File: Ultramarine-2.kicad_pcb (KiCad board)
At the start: 2 copper layers, 135 x 122.8 mm, 148 parts, among them SW1 SW_Push, SW10 SW_Push, SW11 SW_Push, SW12 SW_Push, SW13 SW_Push, SW14 Command 2, SW15 SW_Push, SW16 SW_Push, SW17 SW_Push, SW18 SW_Push, SW19 SW_Push, SW2 SW_Push, SW20 SW_Push, SW21 Command 3, SW22 SW_Push, SW23 SW_Push, SW24 SW_Push, SW25 SW_Push, SW26 SW_Push, SW27 SW_Push, SW28 SW_Push, SW29 SW_Push, SW3 SW_Push, SW30 SW_Push, SW31 Extra, SW32 SW_Push, SW33 SW_Push, SW34 SW_Push, SW35 RotaryEncoder_Switch, SW36 Reset, SW4 SW_Push, SW5 SW_Push, SW6 SW_Push, SW7 Command 1, SW8 SW_Push, SW9 SW_Push

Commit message: Added Qi charging unit
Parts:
- removed D100, D101, D102, D103, D104, D105, D21, D78, D79, D80, D81, D82, D83, D84, D99: D, Diode_SMD:D_SOD-123
- removed D14, D67, D68, D69, D7, D70, D71, D72, D73, D74, D75, D76, D77, D85, D86, D87, D88, D89, D90, D91, D92, D93, D94, D95, D96, D97, D98: SK6812MINI, LED_SMD:LED_SK6812MINI_PLCC4_3.5x3.5mm_P1.75mm
- removed SW14: Command 2, Button_Switch_THT:SW_Tactile_SPST_Angled_PTS645Vx58-2LFS
- removed SW21: Command 3, Button_Switch_THT:SW_Tactile_SPST_Angled_PTS645Vx58-2LFS
- removed SW7: Command 1, Button_Switch_THT:SW_Tactile_SPST_Angled_PTS645Vx58-2LFS
- added J1: OLED, Connector_PinSocket_2.54mm:PinSocket_1x04_P2.54mm_Vertical, F.Cu at (207.2, 80.0)
- added J2: TRRS, Ultramarine-2:MJ-4PP-9, F.Cu at (221.0, 52.0)
- added JP5: Power1, Jumper:SolderJumper-3_P2.0mm_Open_TrianglePad1.0x1.5mm, F.Cu at (161.5, -26.2)
- added JP6: Batt.1, Jumper:SolderJumper-3_P2.0mm_Open_TrianglePad1.0x1.5mm, F.Cu at (161.5, -18.5)
- added JP7: Power1, Jumper:SolderJumper-3_P2.0mm_Open_TrianglePad1.0x1.5mm, F.Cu at (161.5, -22.4)
- added JP8: Batt.2, Jumper:SolderJumper-3_P2.0mm_Open_TrianglePad1.0x1.5mm, F.Cu at (161.5, -14.7)
- added R1: 10K, Resistor_SMD:R_0603_1608Metric, F.Cu at (167.0, -14.5)
- added R2: 10K, Resistor_SMD:R_0603_1608Metric, F.Cu at (167.0, -12.0)
- added REF**: Stabilizer_Cherry_MX_2.00u, PCM_Mounting_Keyboard_Stabilizer:Stabilizer_Cherry_MX_2.00u, F.Cu at (202.9, 134.9)
- added U2: ~, Ultramarine-2:BLE Micro Pro, B.Cu at (152.0, 47.5)
- added U3: ~, Ultramarine-2:BLE Micro Pro, F.Cu at (171.0, 47.5)
- C1: value C -> 0.33u
- C2: value C -> 2.2u
- D1, D10, D11, D12, D13, D2, D22, D23, D24, D25, D26, D27, D28, D29, D3, D30, D31, D32, D33, D34, D35, D4, D5, D6, D8, D9: value SK6812MINI -> D; footprint LED_SMD:LED_SK6812MINI_PLCC4_3.5x3.5mm_P1.75mm -> Ultramarine-2:SOD-123_reversible
- D15, D16, D17, D18, D19, D20: footprint Diode_SMD:D_SOD-123 -> Ultramarine-2:SOD-123_reversible
- D36, D37, D38, D39, D40, D41, D42, D57, D58, D59, D60, D61, D62, D63: value D -> SK6812MINI; footprint Diode_SMD:D_SOD-123 -> Ultramarine-2:SK6812-mini_reversible
- D43, D44, D45, D46, D47, D48, D49, D50, D51, D52, D53, D54, D55, D56, D64, D65: footprint LED_SMD:LED_SK6812MINI_PLCC4_3.5x3.5mm_P1.75mm -> Ultramarine-2:SK6812-mini_reversible
- D66: value SK6812MINI -> D; footprint LED_SMD:LED_SK6812MINI_PLCC4_3.5x3.5mm_P1.75mm -> Diode_SMD:D_SOD-123
- JP2, JP3: moved to B.Cu
- moved D35 233.5 mm to (193.0, 133.0), turned to -30 degrees
- moved D33 225.1 mm to (175.0, 122.0), turned to -30 degrees
- moved D34 223.7 mm to (178.5, 124.0), turned to -30 degrees
- moved D65 218.8 mm to (207.2, 137.4), turned to -120 degrees
- moved D30 217.5 mm to (106.5, 116.5)
- moved D31 213.5 mm to (140.5, 111.5)
- moved D64 210.7 mm to (179.2, 137.9), turned to 150 degrees
- moved D32 209.7 mm to (144.5, 111.5)
- moved D28 205.5 mm to (207.0, 106.5), turned to 90 degrees
- moved D48 193.1 mm to (95.0, 93.0), turned to 180 degrees
- moved D53 191.8 mm to (190.0, 91.0), turned to 180 degrees
- moved D49 189.2 mm to (114.0, 93.0), turned to 180 degrees
- moved D13 186.5 mm to (182.5, 60.5)
- moved D27 186.2 mm to (182.5, 95.5)
- moved D26 185.8 mm to (178.5, 92.5)
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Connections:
- D1 pad 1: Net-(D1-DOUT) -> /R0
- D1 pad 2: GND -> Net-(D1-A)
- D10 pad 1: Net-(D10-DOUT) -> /R1
- D10 pad 2: GND -> Net-(D10-A)
- D11 pad 1: Net-(D11-DOUT) -> /R1
- D11 pad 2: GND -> Net-(D11-A)
- D12 pad 1: Net-(D12-DOUT) -> /R1
- D12 pad 2: GND -> Net-(D12-A)
- D13 pad 1: Net-(D13-DOUT) -> /R1
- D13 pad 2: GND -> Net-(D13-A)
- D15 pad 1: /R0 -> /R2
- D16 pad 1: /R0 -> /R2
- D17 pad 1: /R0 -> /R2
- D18 pad 1: /R0 -> /R2
- D19 pad 1: /R0 -> /R2
- D2 pad 1: Net-(D2-DOUT) -> /R0
- D2 pad 2: GND -> Net-(D2-A)
- D20 pad 1: /R0 -> /R2
- D22 pad 1: Net-(D22-DOUT) -> /R3
- D22 pad 2: GND -> Net-(D22-A)
- D23 pad 1: Net-(D22-DIN) -> /R3
- D23 pad 2: GND -> Net-(D23-A)
- D24 pad 1: Net-(D23-DIN) -> /R3
- D24 pad 2: GND -> Net-(D24-A)
- D25 pad 1: Net-(D24-DIN) -> /R3
- D25 pad 2: GND -> Net-(D25-A)
- D26 pad 1: Net-(D25-DIN) -> /R3
- D26 pad 2: GND -> Net-(D26-A)
- D27 pad 1: Net-(D26-DIN) -> /R3
- D27 pad 2: GND -> Net-(D27-A)
- D28 pad 1: Net-(D27-DIN) -> /R3
- D28 pad 2: GND -> /RE_S2
- D29 pad 1: Net-(D29-DOUT) -> /R4
- D29 pad 2: GND -> Net-(D29-A)
- D3 pad 1: Net-(D3-DOUT) -> /R0
- D3 pad 2: GND -> Net-(D3-A)
- D30 pad 1: Net-(D29-DIN) -> /R4
- D30 pad 2: GND -> Net-(D30-A)
- D31 pad 1: Net-(D30-DIN) -> /R4
- D31 pad 2: GND -> Net-(D31-A)
- D32 pad 1: Net-(D31-DIN) -> /R4
- D32 pad 2: GND -> Net-(D32-A)
- D33 pad 1: Net-(D32-DIN) -> /R4
- D33 pad 2: GND -> Net-(D33-A)
- D34 pad 1: Net-(D33-DIN) -> /R4
- D34 pad 2: GND -> Net-(D34-A)
- D35 pad 1: Net-(D34-DIN) -> /R4
- D35 pad 2: GND -> Net-(D35-A)
- D36 pad 1: /R1 -> Net-(D36-DOUT)
- D36 pad 2: Net-(D36-A) -> GND
- D37 pad 1: /R1 -> Net-(D37-DOUT)
- D37 pad 2: Net-(D37-A) -> GND
- D38 pad 1: /R1 -> Net-(D38-DOUT)
- D38 pad 2: Net-(D38-A) -> GND
- D39 pad 1: /R1 -> Net-(D39-DOUT)
- D39 pad 2: Net-(D39-A) -> GND
- D4 pad 1: Net-(D4-DOUT) -> /R0
- D4 pad 2: GND -> Net-(D4-A)
- D40 pad 1: /R1 -> Net-(D40-DOUT)
- D40 pad 2: Net-(D40-A) -> GND
- D41 pad 1: /R1 -> Net-(D41-DOUT)
- D41 pad 2: Net-(D41-A) -> GND
- D42 pad 1: /R1 -> Net-(D42-DOUT)
- D42 pad 2: Net-(D42-A) -> +5V
- D43 pad 1: Net-(D43-DOUT) -> Net-(D42-DIN)
- D43 pad 2: GND -> +5V
- D43 pad 3: Net-(D22-DOUT) -> Net-(D43-DIN)
- D43 pad 4: +5V -> GND
- D44 pad 1: Net-(D44-DOUT) -> Net-(D43-DIN)
- D44 pad 2: GND -> +5V
- D44 pad 3: Net-(D43-DOUT) -> Net-(D44-DIN)
- D44 pad 4: +5V -> GND
- D45 pad 1: Net-(D45-DOUT) -> Net-(D44-DIN)
- D45 pad 2: GND -> +5V
- D45 pad 3: Net-(D44-DOUT) -> Net-(D45-DIN)
- D45 pad 4: +5V -> GND
- D46 pad 1: Net-(D46-DOUT) -> Net-(D45-DIN)
- D46 pad 2: GND -> +5V
- D46 pad 3: Net-(D45-DOUT) -> Net-(D46-DIN)
- D46 pad 4: +5V -> GND
- D47 pad 1: Net-(D47-DOUT) -> Net-(D46-DIN)
- D47 pad 2: GND -> +5V
- D47 pad 3: Net-(D46-DOUT) -> Net-(D41-DOUT)
- D47 pad 4: +5V -> GND
- D48 pad 3: Net-(D47-DOUT) -> Net-(D42-DOUT)
- D5 pad 1: Net-(D5-DOUT) -> /R0
- D5 pad 2: GND -> Net-(D5-A)
- D50 pad 3: Net-(D29-DOUT) -> Net-(D49-DOUT)
- D54 pad 2: GND -> +5V
- D54 pad 3: Net-(D53-DOUT) -> Net-(D54-DIN)
- D54 pad 4: +5V -> GND
- D55 pad 1: Net-(D55-DOUT) -> Net-(D54-DIN)
- D55 pad 2: GND -> +5V
- D55 pad 3: Net-(D54-DOUT) -> Net-(D55-DIN)
- D55 pad 4: +5V -> GND
- D56 pad 1: Net-(D56-DOUT) -> Net-(D55-DIN)
- D56 pad 2: GND -> +5V
- D56 pad 3: Net-(D55-DOUT) -> Net-(D56-DIN)
- D56 pad 4: +5V -> GND
- D57 pad 1: /R2 -> Net-(D56-DIN)
- D57 pad 2: Net-(D57-A) -> +5V
- D58 pad 1: /R2 -> Net-(D57-DIN)
- D58 pad 2: Net-(D58-A) -> +5V
- D59 pad 1: /R2 -> Net-(D58-DIN)
- D59 pad 2: Net-(D59-A) -> +5V
- D6 pad 1: Net-(D6-DOUT) -> /R0
- D6 pad 2: GND -> Net-(D6-A)
- D60 pad 1: /R2 -> Net-(D60-DOUT)
- D60 pad 2: Net-(D60-A) -> GND
- D61 pad 1: /R2 -> Net-(D61-DOUT)
- D61 pad 2: Net-(D61-A) -> GND
- D62 pad 1: /R2 -> Net-(D62-DOUT)
- D62 pad 2: Net-(D62-A) -> GND
- D63 pad 1: /R2 -> Net-(D63-DOUT)
- D63 pad 2: Net-(D63-A) -> GND
- D64 pad 3: Net-(D64-DIN) -> Net-(D63-DOUT)
- D65 pad 1: Net-(D64-DIN) -> unconnected-(D65-DOUT-Pad1)
- D65 pad 3: Net-(D65-DIN) -> Net-(D64-DOUT)
- D66 pad 1: Net-(D65-DIN) -> +5V
- D66 pad 2: GND -> /Charging
- D8 pad 1: Net-(D8-DOUT) -> /R1
- D8 pad 2: GND -> Net-(D8-A)
- D9 pad 1: Net-(D10-DIN) -> /R1
- D9 pad 2: GND -> Net-(D9-A)
- SW1 pad 2: Net-(D15-A) -> Net-(D1-A)
- SW10 pad 2: Net-(D38-A) -> Net-(D10-A)
- SW11 pad 2: Net-(D39-A) -> Net-(D11-A)
- SW12 pad 2: Net-(D40-A) -> Net-(D12-A)
- SW13 pad 2: Net-(D41-A) -> Net-(D13-A)
- SW15 pad 2: Net-(D57-A) -> Net-(D15-A)
- SW16 pad 2: Net-(D58-A) -> Net-(D16-A)
- SW17 pad 2: Net-(D59-A) -> Net-(D17-A)
- SW18 pad 2: Net-(D60-A) -> Net-(D18-A)
- SW19 pad 2: Net-(D61-A) -> Net-(D19-A)
- SW2 pad 2: Net-(D16-A) -> Net-(D2-A)
- SW20 pad 2: Net-(D62-A) -> Net-(D20-A)
- SW22 pad 2: Net-(D78-A) -> Net-(D22-A)
- SW23 pad 2: Net-(D79-A) -> Net-(D23-A)
- SW24 pad 2: Net-(D80-A) -> Net-(D24-A)
- SW25 pad 2: Net-(D81-A) -> Net-(D25-A)
- SW26 pad 2: Net-(D82-A) -> Net-(D26-A)
- SW27 pad 2: Net-(D83-A) -> Net-(D27-A)
- SW28 pad 2: Net-(D99-A) -> Net-(D29-A)
- SW29 pad 2: Net-(D100-A) -> Net-(D30-A)
- SW3 pad 2: Net-(D17-A) -> Net-(D3-A)
- SW30 pad 2: Net-(D101-A) -> Net-(D31-A)
- SW31 pad 2: Net-(D102-A) -> Net-(D32-A)
- SW32 pad 2: Net-(D103-A) -> Net-(D33-A)
- SW33 pad 2: Net-(D104-A) -> Net-(D34-A)
- SW34 pad 2: Net-(D105-A) -> Net-(D35-A)
- SW36 pad 2: /RESET -> /Reset
- SW4 pad 2: Net-(D18-A) -> Net-(D4-A)
- SW5 pad 2: Net-(D19-A) -> Net-(D5-A)
- SW6 pad 2: Net-(D20-A) -> Net-(D6-A)
- SW8 pad 2: Net-(D36-A) -> Net-(D8-A)
- SW9 pad 2: Net-(D37-A) -> Net-(D9-A)
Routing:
- net /R4: track 0.00 -> 133.0 mm, vias 0 -> 2
- net /R0: track 0.00 -> 131.9 mm, vias 0 -> 5
- net /LED: track 0.00 -> 107.5 mm
- net /SDA: track 0.00 -> 57.8 mm
- net /SCL: track 0.00 -> 55.0 mm, vias 0 -> 1
- net /Bat+: track 0.00 -> 42.2 mm
- net Net-(D64-DOUT): track 0.00 -> 38.1 mm, vias 0 -> 1
- net Net-(D54-DOUT): track 0.00 -> 36.1 mm, vias 0 -> 2
- net Net-(D41-DOUT): track 0.00 -> 34.9 mm, vias 0 -> 2
- net Net-(D53-DOUT): track 0.00 -> 34.9 mm, vias 0 -> 2
- net Net-(D42-DOUT): track 0.00 -> 34.4 mm, vias 0 -> 2
- net Net-(D61-DOUT): track 0.00 -> 31.0 mm, vias 0 -> 2
- net Net-(D62-DOUT): track 0.00 -> 29.3 mm, vias 0 -> 1
- net Net-(D50-DOUT): track 0.00 -> 26.5 mm, vias 0 -> 2
- net Net-(D51-DOUT): track 0.00 -> 26.5 mm, vias 0 -> 2
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
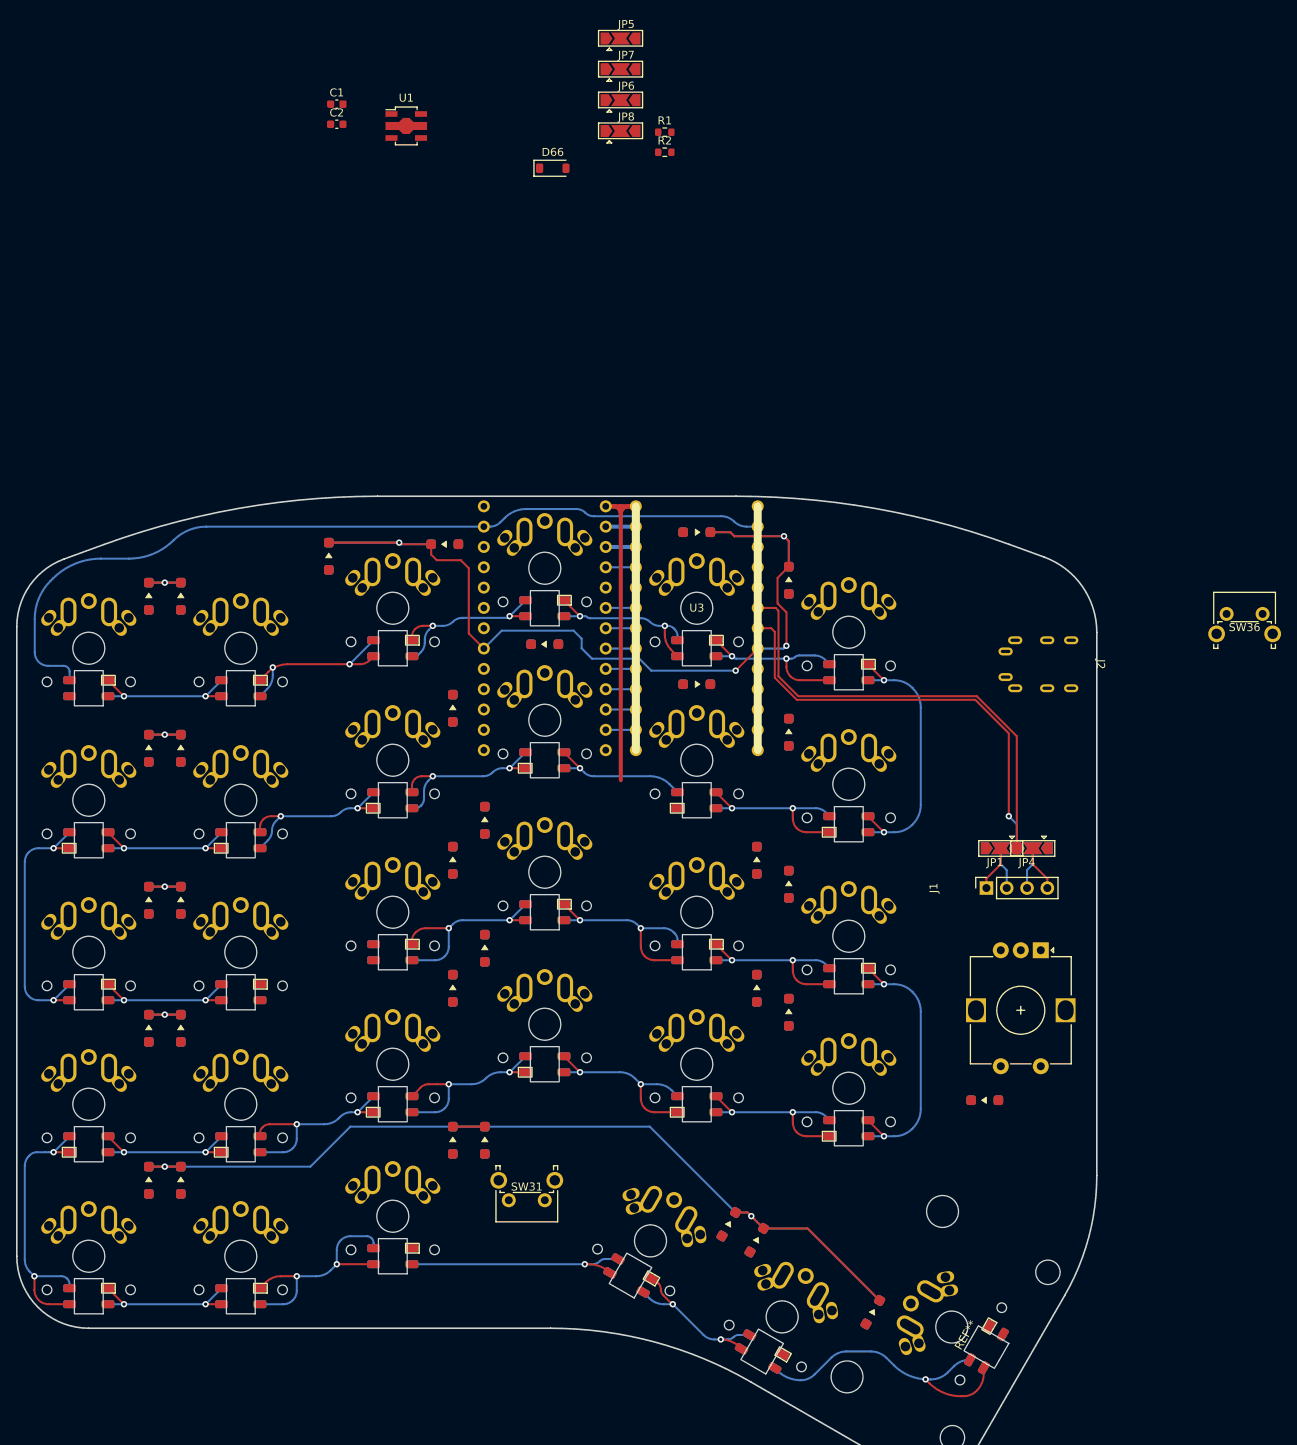
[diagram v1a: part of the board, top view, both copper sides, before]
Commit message: add PCB patterns
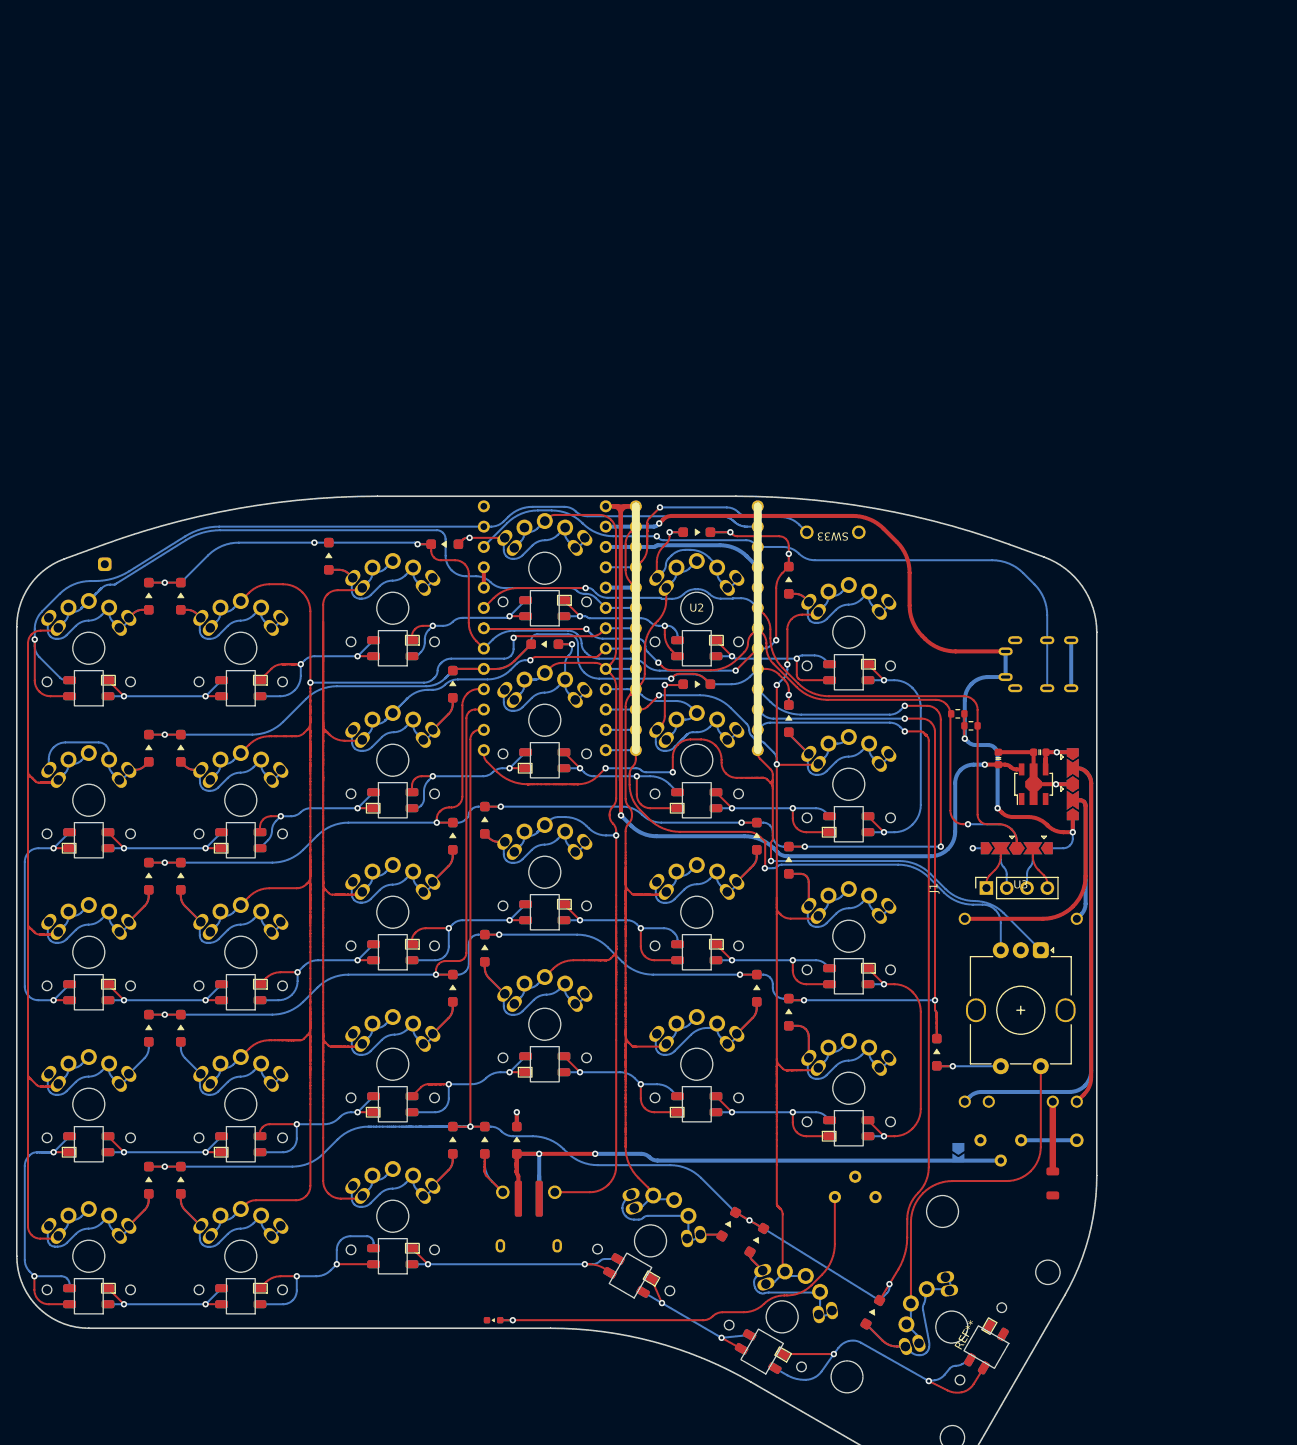
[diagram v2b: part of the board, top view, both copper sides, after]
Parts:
- removed the U1 at (134.7, -15.3)
- added BT1: Qi Charging Unit, Ultramarine-2:Micro_USB_Charging, F.Cu at (150.0, 124.7)
- added D64: Power (WH), Ultramarine-2:LED1608_reversible, F.Cu at (145.6, 134.0)
- added F1: Polyfuse_Small, Ultramarine-2:MF-NSMF, F.Cu at (215.5, 116.9)
- added J3: Flexible LED 3V, Connector_PinSocket_2.54mm:PinSocket_1x01_P2.54mm_Vertical, F.Cu at (218.5, 111.5)
- added J4: Flexible LED GND, Connector_PinSocket_2.54mm:PinSocket_1x01_P2.54mm_Vertical, F.Cu at (97.0, 39.5)
- added JP9: Flex LED for Power, Jumper:SolderJumper-2_P1.3mm_Open_TrianglePad1.0x1.5mm, B.Cu at (203.7, 113.1)
- added RV1: 10K, Ultramarine-2:R_variable, F.Cu at (190.8, 118.6)
- added RV2: 10K, Ultramarine-2:R_variable, F.Cu at (209.0, 111.5)
- added U3: ~, Ultramarine-2:TP4056, F.Cu at (211.5, 95.2)
- added U4: ~, Package_TO_SOT_SMD:SOT-89-5, F.Cu at (213.1, 67.0)
- D63: renamed from D66; footprint Diode_SMD:D_SOD-123 -> Ultramarine-2:SOD-123_reversible
- JP1, JP2, JP3, JP4, JP7: footprint Jumper:SolderJumper-3_P2.0mm_Open_TrianglePad1.0x1.5mm -> Ultramarine-2:Jumper 3pin
- JP5: renamed from JP6; footprint Jumper:SolderJumper-3_P2.0mm_Open_TrianglePad1.0x1.5mm -> Ultramarine-2:Jumper 3pin
- JP6: renamed from JP5; footprint Jumper:SolderJumper-3_P2.0mm_Open_TrianglePad1.0x1.5mm -> Ultramarine-2:Jumper 3pin; moved to B.Cu
- JP8: footprint Jumper:SolderJumper-3_P2.0mm_Open_TrianglePad1.0x1.5mm -> Ultramarine-2:Jumper 3pin; moved to B.Cu
- SW28: renamed from SW31; footprint Button_Switch_THT:SW_Tactile_SPST_Angled_PTS645Vx58-2LFS -> Ultramarine-2:Tactlie_Switch
- SW33: renamed from SW36; footprint Button_Switch_THT:SW_Tactile_SPST_Angled_PTS645Vx58-2LFS -> Ultramarine-2:Tactlie_Switch
- moved D63 121.6 mm to (148.5, 111.5)
- moved C1 119.5 mm to (213.9, 63.0), turned to 180 degrees
- moved C2 114.6 mm to (208.7, 63.8), turned to 90 degrees
- moved JP6 110.7 mm to (218.0, 69.0), turned to 90 degrees
- moved JP7 107.4 mm to (218.0, 69.0), turned to -90 degrees
- moved JP5 100.8 mm to (218.0, 65.0), turned to -90 degrees
- moved JP8 97.7 mm to (218.0, 65.0), turned to 90 degrees
- moved R1 83.5 mm to (205.3, 59.7)
- moved R2 79.2 mm to (203.6, 58.2), turned to 180 degrees
- moved SW33 50.3 mm to (188.0, 35.5), turned to 180 degrees
- moved D25 8.49 mm to (201.0, 100.5), turned to 0 degrees
- moved D13 3.00 mm to (102.5, 78.5)
- moved D14 3.00 mm to (106.5, 78.5)
- moved D15 3.00 mm to (140.5, 73.5)
- moved D17 3.00 mm to (178.5, 73.5)
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- renumbered D11 to D10, D12 to D11, D13 to D12, D15 to D13, D16 to D14, D17 to D15, D18 to D16, D19 to D17, D20 to D18, D22 to D19, D23 to D20, D24 to D21, D25 to D22, D26 to D23, D27 to D24, D28 to D25, D29 to D26, D30 to D27, D31 to D28, D32 to D29, D33 to D30, D34 to D31, D35 to D32, D36 to D33, D37 to D34, D38 to D35, D39 to D36, D40 to D37, D41 to D38, D42 to D39, D43 to D40, D44 to D41, D45 to D42, D46 to D43, D47 to D44, D48 to D45, D49 to D46, D50 to D47, D51 to D48, D52 to D49, D53 to D50, D54 to D51, D55 to D52, D56 to D53, D57 to D54, D58 to D55, D59 to D56, D60 to D57, D61 to D58, D62 to D59, D63 to D60, D64 to D61, D65 to D62, D8 to D7, D9 to D8, D10 to D9, SW11 to SW10, SW12 to SW11, SW13 to SW12, SW15 to SW13, SW16 to SW14, SW17 to SW15, SW18 to SW16, SW19 to SW17, SW20 to SW18, SW22 to SW19, SW23 to SW20, SW24 to SW21, SW25 to SW22, SW26 to SW23, SW27 to SW24, SW28 to SW25, SW29 to SW26, SW30 to SW27, SW32 to SW29, SW33 to SW30, SW34 to SW31, SW35 to SW32, SW8 to SW7, SW9 to SW8, SW10 to SW9, U2 to U1, U3 to U2
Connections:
- C1 pad 1: Net-(JP6-C) -> Net-(JP5-A)
- JP2 pad 3: +3.3V -> +5V
- JP3 pad 1: +3.3V -> +5V
- JP5 pad 1: Net-(JP6-A) -> Net-(JP5-A)
- JP5 pad 2: Net-(JP6-C) -> Net-(JP5-C)
- JP5 pad 3: Net-(JP6-B) -> GND
- JP6 pad 1: GND -> +5V
- JP6 pad 2: + -> Net-(JP6-C)
- JP6 pad 3: +5V -> GND
- JP7 pad 1: +5V -> GND
- JP7 pad 2: - -> Net-(JP7-C)
- JP7 pad 3: GND -> +5V
- JP8 pad 1: Net-(JP8-A) -> GND
- JP8 pad 2: Net-(JP6-C) -> Net-(JP8-C)
- JP8 pad 3: Net-(JP6-A) -> Net-(JP5-A)
- U1 pad 12: unconnected-(U2-B5-Pad12) -> /RE_A
- U1 pad 13: unconnected-(U2-B6-Pad13) -> /RE_B
- U2 pad 12: unconnected-(U3-B5-Pad12) -> /RE_A
- U2 pad 13: unconnected-(U3-B6-Pad13) -> /RE_B
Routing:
- net /R3: track 8.00 -> 231.1 mm, vias 1 -> 7
- net /C0: track 3.76 -> 206.2 mm
- net /C1: track 3.76 -> 200.2 mm, vias 0 -> 2
- net /C2: track 3.76 -> 184.1 mm, vias 0 -> 1
- net /R2: track 8.00 -> 177.3 mm, vias 1 -> 7
- net /C5: track 3.76 -> 162.0 mm, vias 0 -> 4
- net /C3: track 3.76 -> 158.8 mm, vias 0 -> 1
- net /C4: track 3.76 -> 134.7 mm
- net /R4: track 133.0 -> 258.9 mm, vias 2 -> 5
- net +5V: track 3.76 -> 127.1 mm, vias 0 -> 6
- net /R1: track 8.00 -> 115.2 mm, vias 1 -> 3
- net /RE_A: track 0.00 -> 98.3 mm, vias 0 -> 3
- net /data: track 0.00 -> 86.5 mm, vias 0 -> 1
- net /Charging: track 0.00 -> 77.5 mm, vias 0 -> 2
- net /RE_B: track 0.00 -> 67.9 mm, vias 0 -> 1
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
